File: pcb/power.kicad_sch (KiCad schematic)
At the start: 36 parts, among them SW4 SKRPACE010, U32 TPS62237DRYR, U33 BQ24073RGTR, U34 LP5907MFX-3.3/NOPB, U35 TPS3840DL35DBVR, U36 TPS61023DRLR

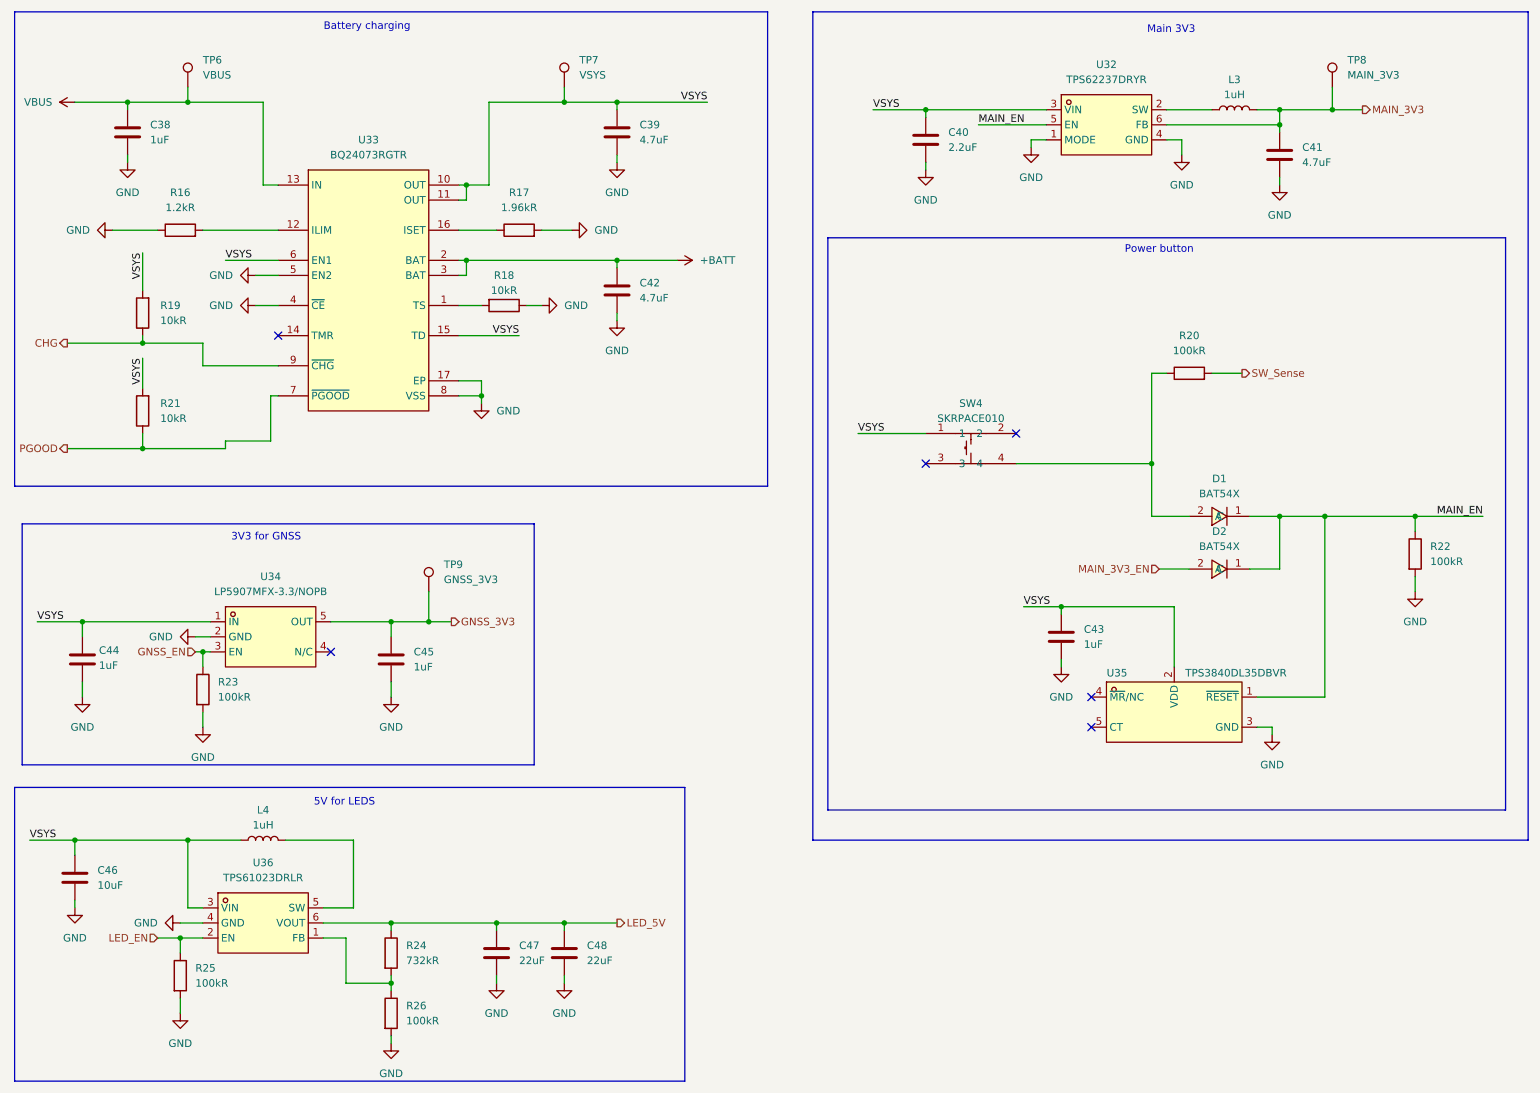
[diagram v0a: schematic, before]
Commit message: Started with firmware, missing display, navigation and leds
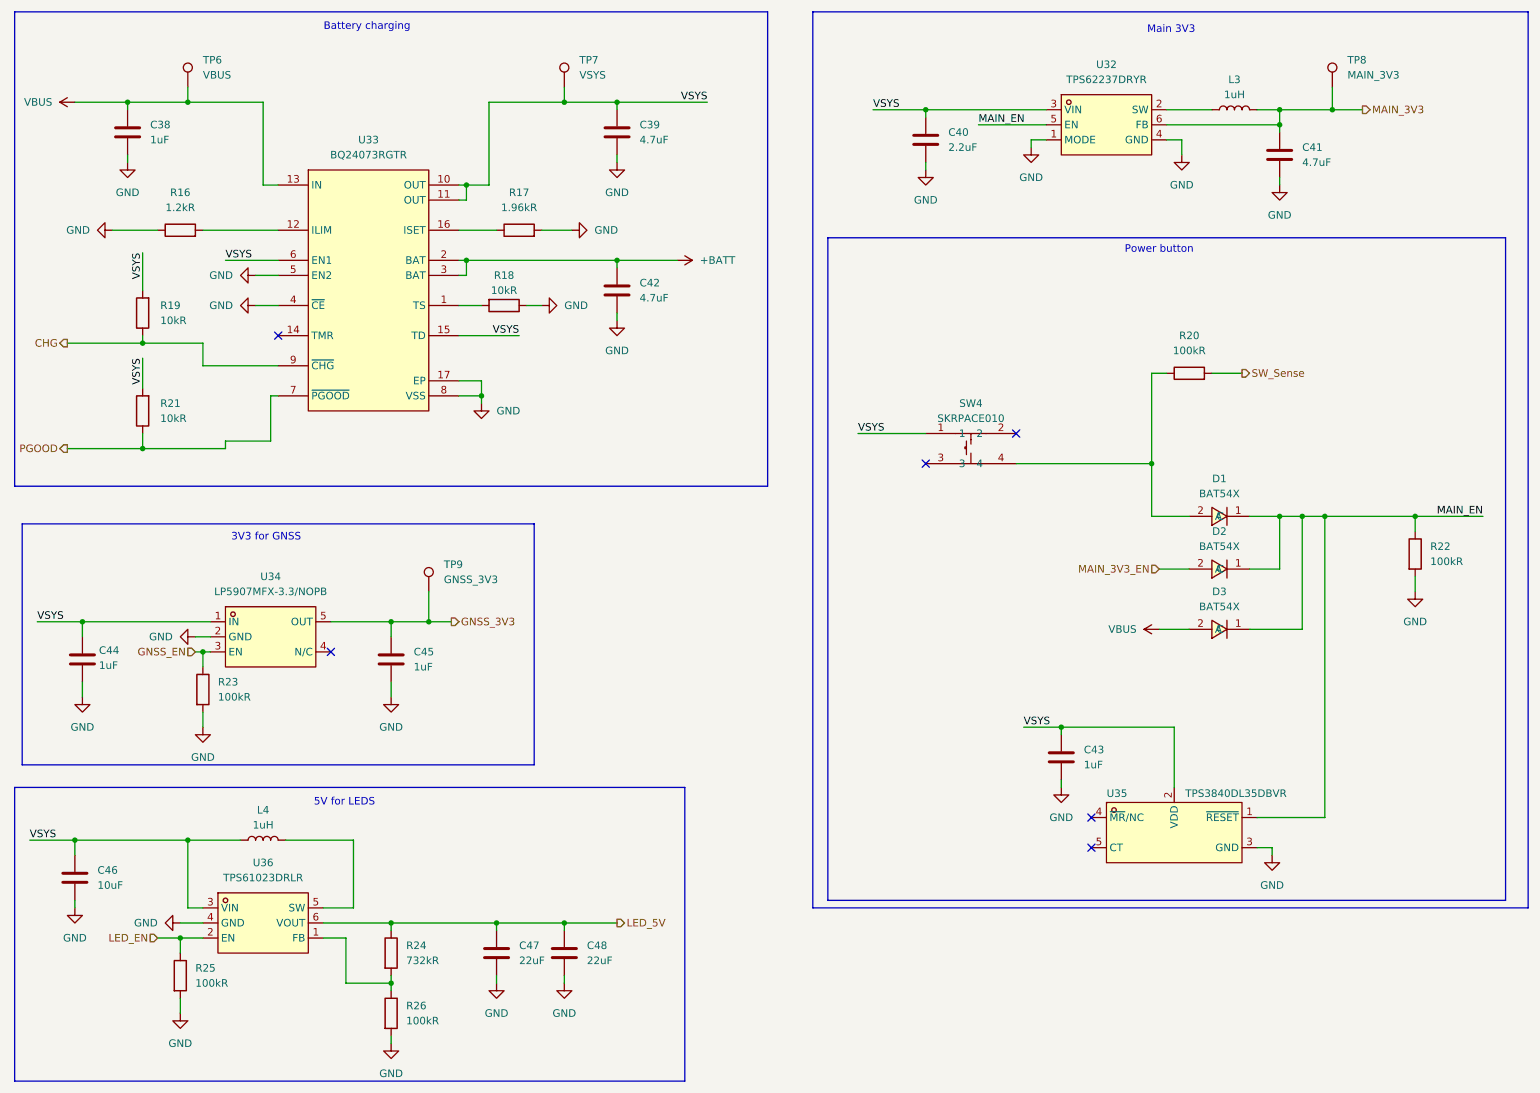
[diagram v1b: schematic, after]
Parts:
- added D3: BAT54X, lcsc_lib:SOD-523_L1.2-W0.8-LS1.6-RD, symbol lcsc:BAT54X_C51315114
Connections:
- net MAIN_EN: now also D3.1 (C)
- net VBUS: now also D3.2 (A)
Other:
- moved on the sheet: C43, U35
